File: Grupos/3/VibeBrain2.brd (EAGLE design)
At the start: 37 x 18 mm, 37 parts, among them J1 TC2030-IDC, U1 TPS62203DBVR, U2 DRV2605LDGSR, U3 MCP73831T-2ACI/OT

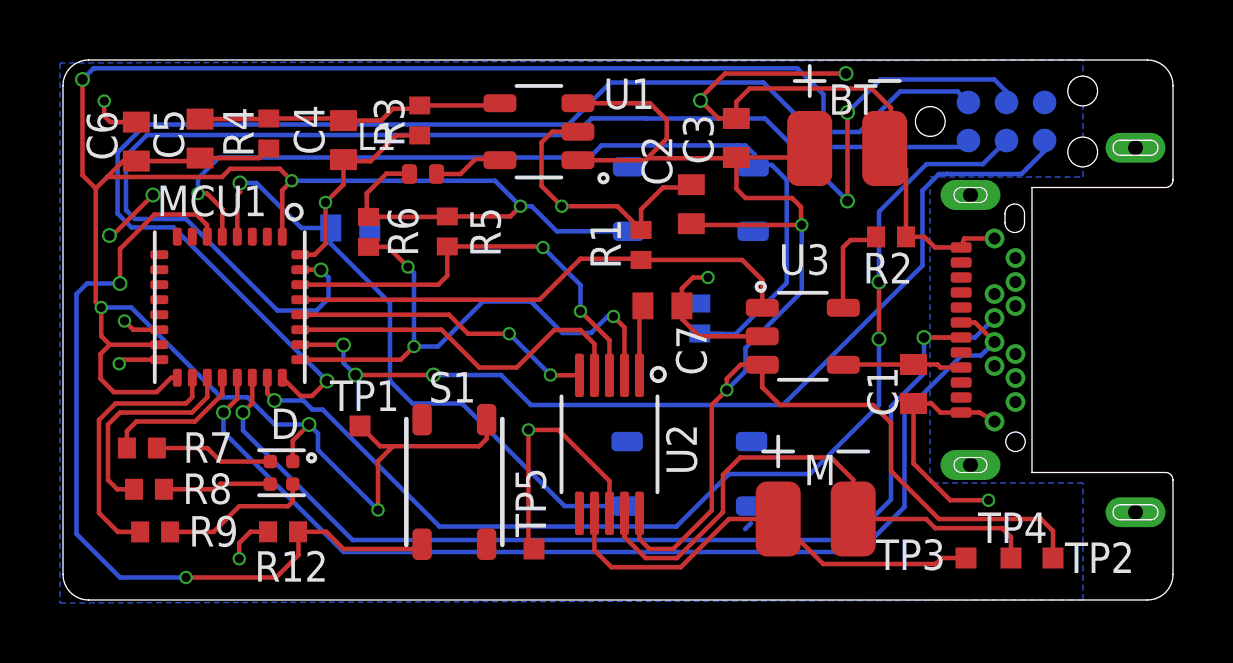
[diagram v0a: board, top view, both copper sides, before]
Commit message: Se agregan resistencias de CC, sin embargo una debe ser cableada manualmente
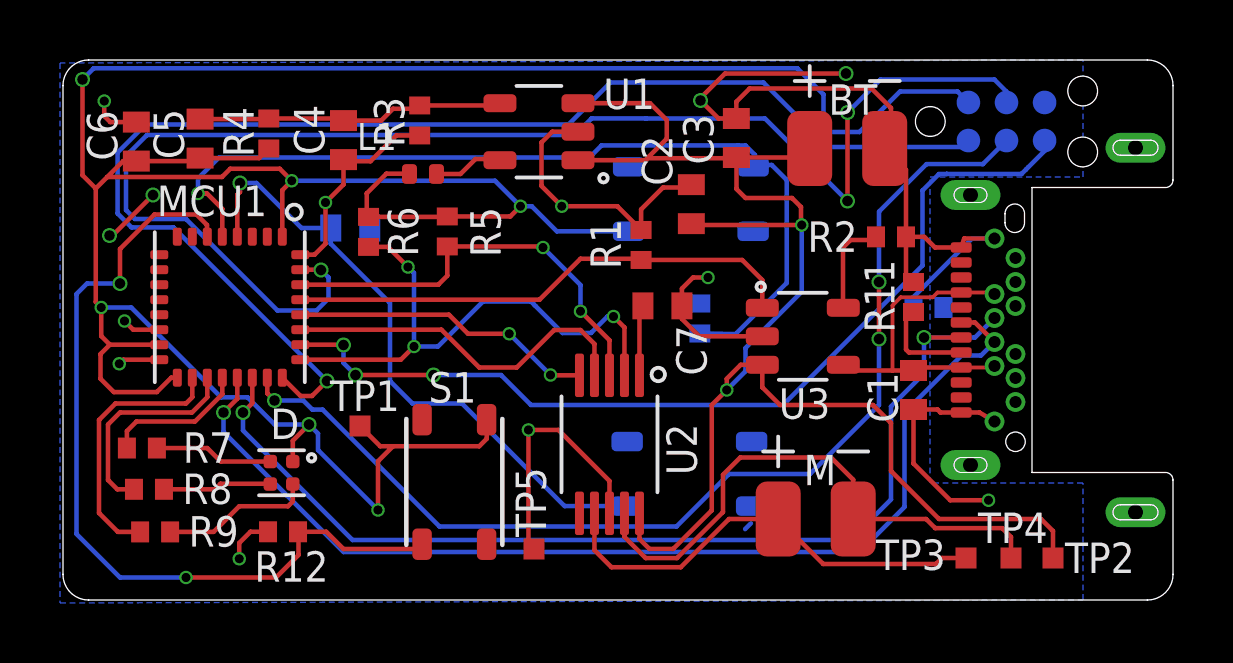
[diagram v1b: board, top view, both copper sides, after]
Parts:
- added R11, R13: 5K1, rcl:R0402
- moved C1 0.20 mm to (28.4, 7.00)
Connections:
- new net N$25: R11.1, USB_C.A5
- new net N$26: R13.1, USB_C.B5
- net GND: now also R11.2, R13.2
- net VDD: now also USB_C.A9, USB_C.B4, USB_C.B9
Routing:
- net VDD: track 3.98 -> 10.9 mm
- net GND: track 64.9 -> 70.1 mm
- net N$25: track 0.00 -> 3.23 mm

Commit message: FAltó guardar
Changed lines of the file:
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@@
 <polygon width="0.1524" layer="16">
 <vertex x="-0.1" y="17.9"/>
-<vertex x="-0.1" y="-0.1"/>
-<vertex x="34" y="0"/>
+<vertex x="-0.1" y="-0.049853125"/>
+<vertex x="34" y="0.050146875"/>
 <vertex x="34" y="3.9"/>
 <vertex x="28.9" y="3.9"/>
@@
 <wire x1="30.3" y1="12.05" x2="31.05" y2="12.05" width="0.1524" layer="16"/>
 <wire x1="28.35" y1="10.1" x2="30.3" y2="12.05" width="0.1524" layer="16"/>
-<wire x1="22.955" y1="5.28" x2="22.93" y2="2.555" width="0" layer="19" extent="16-16"/>
 </signal>
 <signal name="VDD">
@@
 <wire x1="7.05" y1="6.65" x2="8.00738125" y2="6.65" width="0.1524" layer="16"/>
 <wire x1="8.00738125" y1="6.65" x2="8.31178125" y2="6.3456" width="0.1524" layer="16"/>
-<wire x1="22.2" y1="4.2" x2="24.9" y2="4.2" width="0.1524" layer="16"/>
-<wire x1="24.9" y1="4.2" x2="27.2" y2="6.5" width="0.1524" layer="16"/>
-<wire x1="27.2" y1="6.5" x2="27.2" y2="8.7" width="0.1524" layer="16"/>
+<wire x1="22.2" y1="4.2" x2="24.3" y2="4.2" width="0.1524" layer="16"/>
+<wire x1="24.3" y1="4.2" x2="27.2" y2="7.1" width="0.1524" layer="16"/>
+<wire x1="27.2" y1="7.1" x2="27.2" y2="8.7" width="0.1524" layer="16"/>
 <via x="27.2" y="8.7" extent="1-16" drill="0.35"/>
 <via x="27.2" y="10.6" extent="1-16" drill="0.35"/>
@@
 <contactref element="J1" pad="6"/>
 <wire x1="32.72" y1="15.315" x2="32.72" y2="14.97" width="0.1524" layer="16"/>
-<wire x1="32.72" y1="14.97" x2="32.175" y2="14.425" width="0.1524" layer="16"/>
-<wire x1="32.175" y1="14.425" x2="32.1" y2="14.35" width="0.1524" layer="16"/>
+<wire x1="32.72" y1="14.97" x2="31.9532" y2="14.2032" width="0.1524" layer="16"/>
 <wire x1="29.458725" y1="14.2032" x2="29.455525" y2="14.2" width="0.1524" layer="16"/>
 <wire x1="29.455525" y1="14.2" x2="29.2" y2="14.2" width="0.1524" layer="16"/>
-<wire x1="32.1" y1="14.35" x2="31.9532" y2="14.2032" width="0.1524" layer="16"/>
 <wire x1="31.9532" y1="14.2032" x2="29.458725" y2="14.2032" width="0.1524" layer="16"/>
 <wire x1="29.2" y1="14.2" x2="28.65" y2="13.65" width="0.1524" layer="16"/>
 <wire x1="28.65" y1="13.65" x2="28.65" y2="11.15" width="0.1524" layer="16"/>
-<wire x1="28.65" y1="11.15" x2="24" y2="6.5" width="0.1524" layer="16"/>
-<wire x1="24" y1="6.5" x2="15.6" y2="6.5" width="0.1524" layer="16"/>
-<wire x1="15.6" y1="6.5" x2="14.6" y2="7.5" width="0.1524" layer="16"/>
+<wire x1="28.65" y1="11.15" x2="27.1" y2="9.6" width="0.1524" layer="16"/>
+<wire x1="22.75" y1="6.2" x2="15.9" y2="6.2" width="0.1524" layer="16"/>
+<wire x1="15.9" y1="6.2" x2="14.6" y2="7.5" width="0.1524" layer="16"/>
 <wire x1="14.6" y1="7.5" x2="12.35" y2="7.5" width="0.1524" layer="16"/>
 <via x="12.35" y="7.5" extent="1-16" drill="0.35"/>
@@
 <wire x1="7.91" y1="8.51" x2="9.34" y2="8.51" width="0.1524" layer="1"/>
 <wire x1="9.34" y1="8.51" x2="9.35" y2="8.5" width="0.1524" layer="1"/>
+<wire x1="27.1" y1="9.6" x2="26.3" y2="9.6" width="0.127" layer="16"/>
+<wire x1="22.9" y1="6.2" x2="22.75" y2="6.2" width="0.127" layer="16"/>
+<wire x1="26.3" y1="9.6" x2="22.9" y2="6.2" width="0.127" layer="16"/>
 </signal>
 <signal name="N$19">
